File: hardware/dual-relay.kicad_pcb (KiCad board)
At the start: 2 copper layers, 40 x 40 mm, 34 parts, among them P1 CON-SENSOR2, P2 BOOT, P3 CONN_8, P4 Debug, Q1 SSM6N7002KFU, U1 XMC1XXX24, U2 G5LE-1-36, U3 G5LE-1-36, U4 DRILL, U5 DRILL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

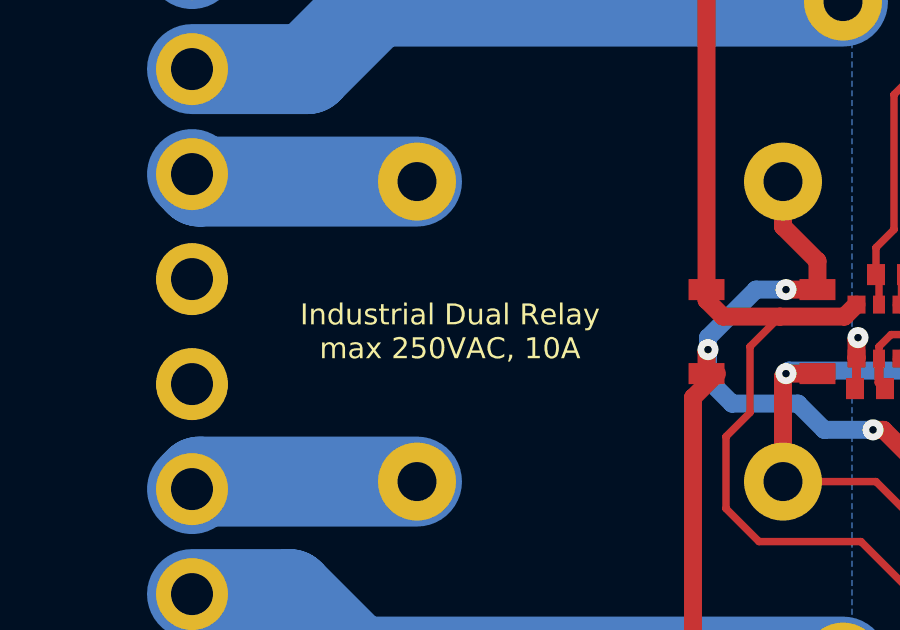
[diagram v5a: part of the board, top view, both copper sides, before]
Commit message: fix tf text, add version number
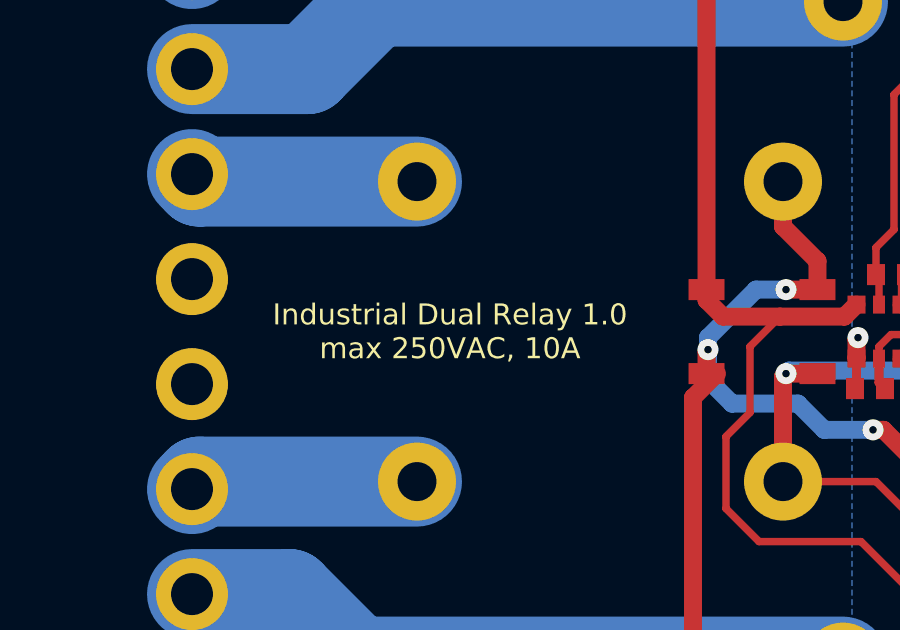
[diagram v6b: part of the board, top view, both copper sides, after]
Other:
- board text added: "Industrial Dual Relay 1.0 max 250VAC, 10A"
- board text removed: "Industrial Dual Relay max 250VAC, 10A"
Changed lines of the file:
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@@
   )
   (layers
-    (0 Vorderseite signal)
+    (0 Vorderseite signal hide)
     (31 Rückseite signal hide)
     (32 B.Adhes user)
@@
     (aux_axis_origin 172.075 124.175)
     (grid_origin 172.075 124.175)
-    (visible_elements FFFFFFBF)
+    (visible_elements FFFF7FBF)
     (pcbplotparams
       (layerselection 0x010f8_80000001)
@@
     (effects (font (size 0.8001 0.8001) (thickness 0.200025)))
   )
-  (gr_text tinkerforge.com (at 166.075 104.175 90) (layer B.SilkS)
+  (gr_text tinkerforge.com (at 166.075 104.175 270) (layer B.SilkS)
     (effects (font (size 1.00076 1.00076) (thickness 0.14986)) (justify mirror))
   )
@@
   (gr_arc (start 169.57294 121.67298) (end 172.0723 121.67298) (angle 90) (layer Edge.Cuts) (width 0.2))
   (gr_arc (start 169.57294 86.67306) (end 169.57294 84.17116) (angle 90) (layer Edge.Cuts) (width 0.2))
-  (gr_text "Industrial Dual Relay\nmax 250VAC, 10A" (at 148.675 104.175) (layer F.SilkS)
+  (gr_text "Industrial Dual Relay 1.0\nmax 250VAC, 10A" (at 148.675 104.175) (layer F.SilkS)
     (effects (font (size 0.7 0.7) (thickness 0.15)))
   )
